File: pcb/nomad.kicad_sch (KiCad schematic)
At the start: 39 parts, among them J1 USB_C_Receptacle_USB2.0_16P, J5 Conn_01x02_Pin, SW1 UP, SW2 DOWN, SW3 RIGHT, SW4 LEFT, SW5 SEL, SW6 SW_Push, SW7 SW_Push, U1 ESP32-S3-WROOM-1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

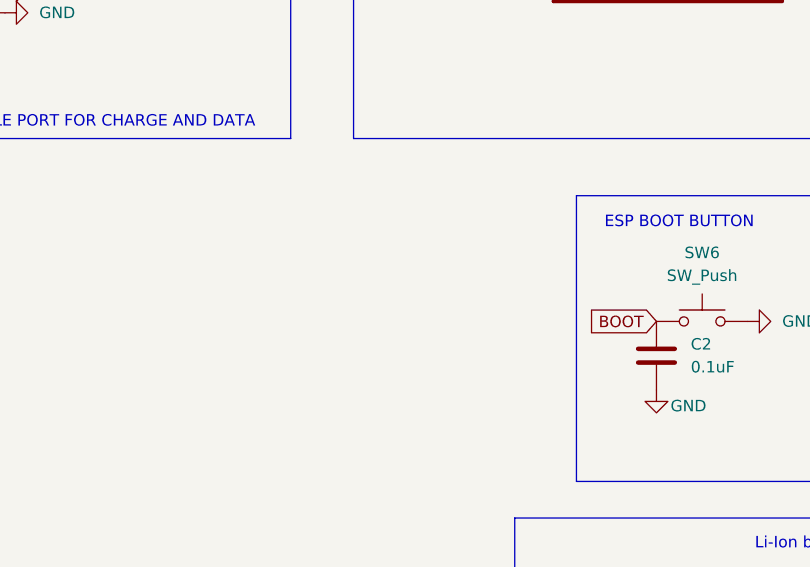
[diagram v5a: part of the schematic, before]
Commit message: Updating footprints, PCb and schematics.
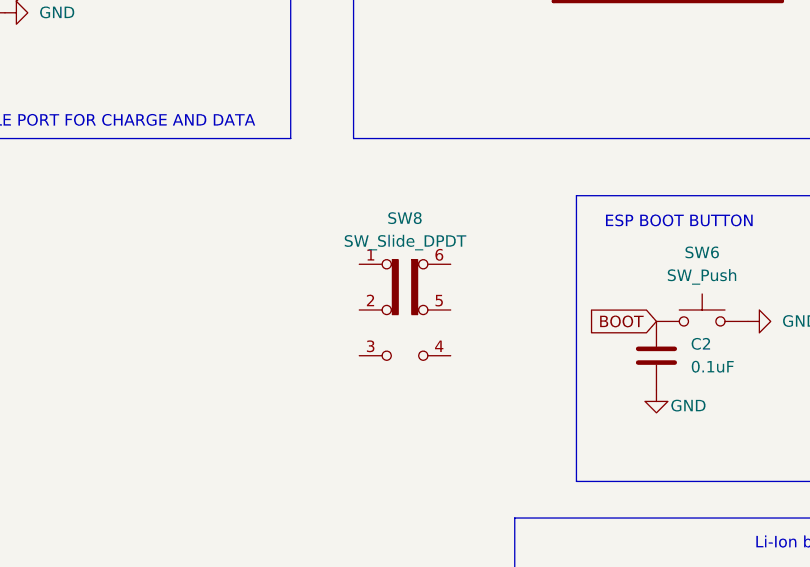
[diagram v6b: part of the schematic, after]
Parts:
- added SW8: SW_Slide_DPDT, symbol Switch:SW_Slide_DPDT
- C12: footprint (none) -> Capacitor_SMD:C_0805_2012Metric
- R18: footprint (none) -> Resistor_SMD:R_0805_2012Metric
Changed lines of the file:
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@@
 			)
 		)
-		(property "Footprint" ""
+		(property "Footprint" "Resistor_SMD:R_0805_2012Metric"
 			(at 225.552 127 90)
 			(hide yes)
@@
 			)
 		)
-		(property "Footprint" ""
+		(property "Footprint" "Capacitor_SMD:C_0805_2012Metric"
 			(at 164.7952 43.18 0)
 			(hide yes)
@@
 					(unit 1)
 				)
+			)
+		)
+	)
+	(symbol
+		(lib_id "Switch:SW_Slide_DPDT")
+		(at 95.25 92.71 0)
+		(unit 1)
+		(body_style 1)
+		(exclude_from_sim no)
+		(in_bom yes)
+		(on_board yes)
+		(in_pos_files yes)
+		(dnp no)
+		(fields_autoplaced yes)
+		(property "Reference" "SW8"
+			(at 95.25 82.55 0)
+			(show_name no)
+			(do_not_autoplace no)
+			(effects
+				(font
+					(size 1.27 1.27)
+				)
+			)
+		)
+		(property "Value" "SW_Slide_DPDT"
+			(at 95.25 85.09 0)
+			(show_name no)
+			(do_not_autoplace no)
+			(effects
+				(font
+					(size 1.27 1.27)
+				)
+			)
+		)
+		(property "Footprint" ""
+			(at 109.22 87.63 0)
+			(hide yes)
+			(show_name no)
+			(do_not_autoplace no)
+			(effects
+				(font
+					(size 1.27 1.27)
+				)
+			)
+		)
+		(property "Datasheet" ""
+			(at 95.25 92.71 0)
+			(hide yes)
+			(show_name no)
+			(do_not_autoplace no)
+			(effects
+				(font
+					(size 1.27 1.27)
+				)
+			)
+		)
+		(property "Description" "Slide Switch, dual pole double throw"
+			(at 95.25 92.71 0)
+			(hide yes)
+			(show_name no)
+			(do_not_autoplace no)
+			(effects
+				(font
+					(size 1.27 1.27)
+				)
+			)
+		)
+		(pin "1"
+		)
+		(pin "4"
+		)
+		(pin "2"
+		)
+		(pin "3"
+		)
+		(pin "6"
+		)
+		(pin "5"
+		)
+		(instances
+			(project "nomad"
+				(path "/76473bbd-feb6-4b7c-8160-a4d55fa11a55"
+					(reference "SW8")
+					(unit 1)
+				)

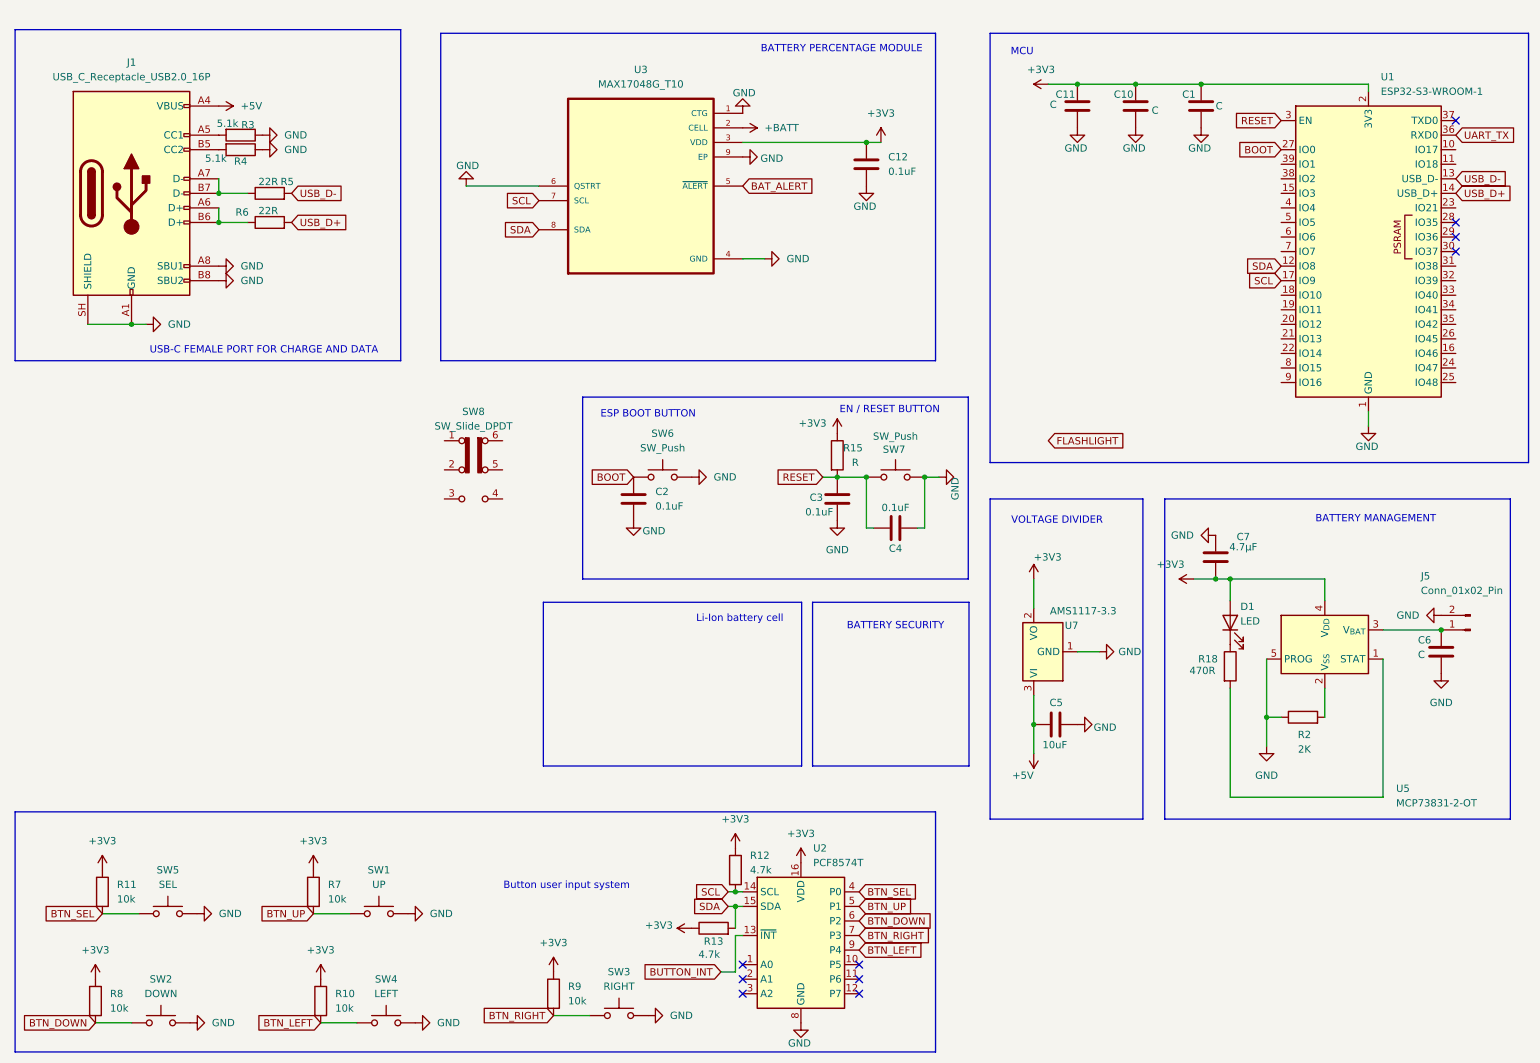
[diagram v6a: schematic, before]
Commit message: Updating PCB: Adding Buck boost converter, battery protection and other fixes.
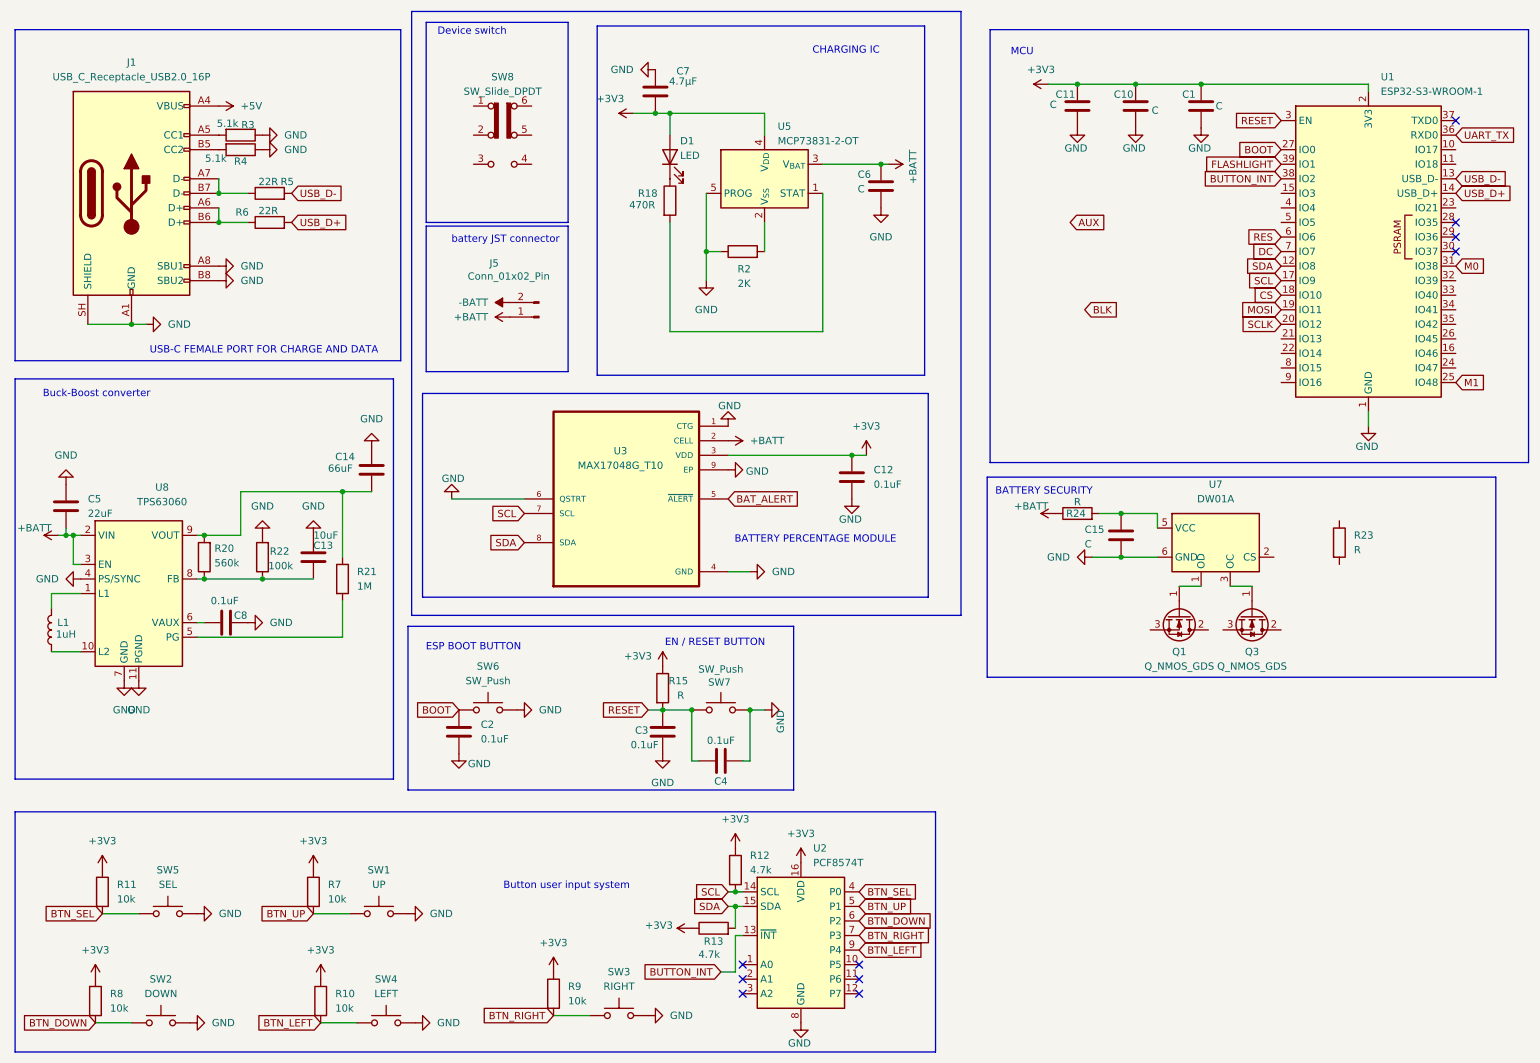
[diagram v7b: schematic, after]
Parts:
- removed U7: AMS1117-3.3, Package_TO_SOT_SMD:SOT-223-3_TabPin2, symbol Regulator_Linear:AMS1117-3.3
- added C13: 10uF, Capacitor_SMD:C_0805_2012Metric, symbol Device:C
- added C14: 66uF, Capacitor_SMD:C_0805_2012Metric, symbol Device:C
- added C15: C, symbol Device:C
- added C8: 0.1uF, Capacitor_SMD:C_0805_2012Metric, symbol Device:C
- added L1: 1uH, Inductor_SMD:L_Coilcraft_XxL4020, symbol Device:L
- added Q1, Q3: Q_NMOS_GDS, symbol Transistor_FET:Q_NMOS_GDS
- added R20: 560k, Resistor_SMD:R_0805_2012Metric, symbol Device:R
- added R21: 1M, Resistor_SMD:R_0805_2012Metric, symbol Device:R
- added R22: 100k, Resistor_SMD:R_0805_2012Metric, symbol Device:R
- added R23, R24: R, symbol Device:R
- added U7: DW01A, Package_TO_SOT_SMD:SOT-23-6, symbol Battery_Management:DW01A
- added U8: TPS63060, Package_SON:Texas_S-PWSON-N10_ThermalVias, symbol Regulator_Switching:TPS63060
- C1, C10, C11: footprint (none) -> Capacitor_SMD:C_0805_2012Metric
- C5: value 10uF -> 22uF
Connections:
- net +5V: no longer C5.1
- net +BATT: now also C5.2, C6.1, J5.1 (Pin_1), U5.3 (V_{BAT}), R24.1, U8.2 (VIN), U8.3 (EN)
- net BUTTON_INT: now also U1.38 (IO2)
- net FLASHLIGHT: now also U1.39 (IO1)
- net GND: now also C5.1, C13.1, C14.1, C15.2, C8.2, R22.2, U7.6 (GND), U8.11 (PGND), U8.4 (PS/SYNC), U8.7 (GND); no longer C5.2, J5.2 (Pin_2)
- net CS: now reaches U1.18 (IO10)
- net MOSI: now reaches U1.19 (IO11)
- net SCLK: now reaches U1.20 (IO12)
- net M1: now reaches U1.25 (IO48)
- net M0: now reaches U1.31 (IO38)
- net RES: now reaches U1.6 (IO6)
- net DC: now reaches U1.7 (IO7)
- new net: L1.2, U8.1 (L1)
- new net: L1.1, U8.10 (L2)
- new net: R21.2, U8.5 (PG)
- new net: C8.1, U8.6 (VAUX)
- new net: C13.2, R20.1, R22.1, U8.8 (FB)
- new net: C14.2, R20.2, R21.1, U8.9 (VOUT)
- new net: Q1.1 (G), U7.1 (OD)
- new net: Q3.1 (G), U7.3 (OC)
- new net: C15.1, R24.2, U7.5 (VCC)
- new net -BATT: J5.2 (Pin_2)
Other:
- note added: "Buck-Boost converter"
- note added: "CHARGING IC"
- note added: "Device switch"
- note added: "battery JST connector"
- note removed: "BATTERY MANAGEMENT"
- note removed: "Li-Ion battery cell"
- note removed: "VOLTAGE DIVIDER"
- moved on the sheet: C12, C2, C3, C4, C6, C7, D1, J5, R15, R18, R2, SW6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

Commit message: Updating PCB: Removing battery security and adding slide switch
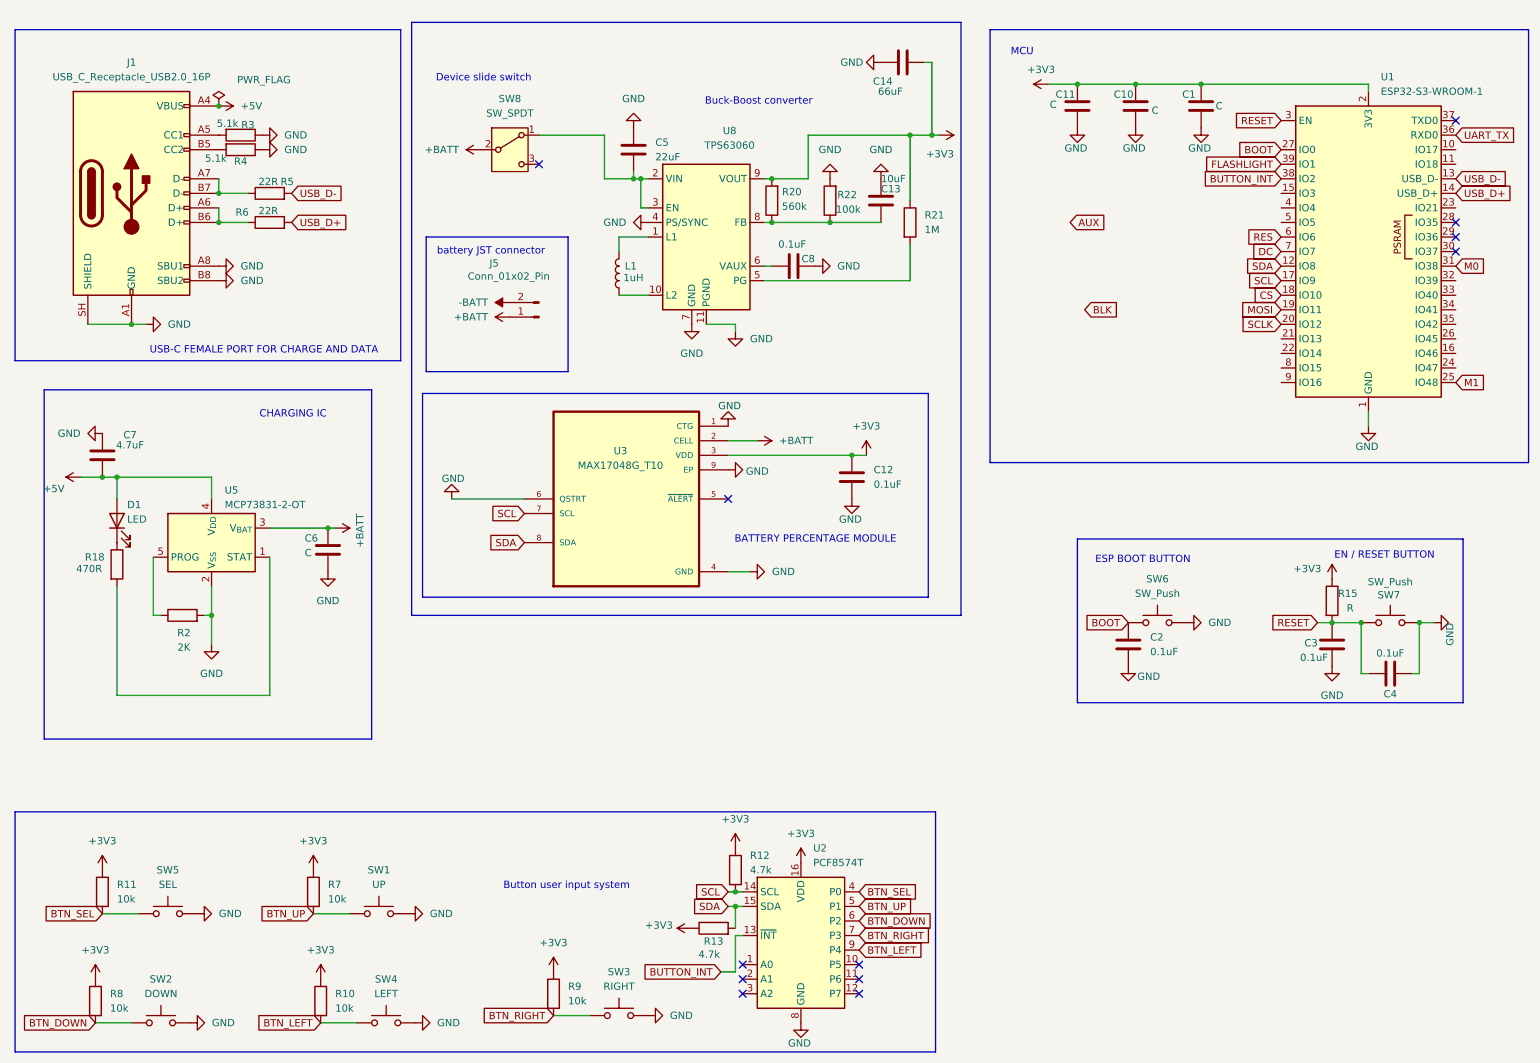
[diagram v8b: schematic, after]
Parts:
- removed C15: C, symbol Device:C
- removed Q1, Q3: Q_NMOS_GDS, symbol Transistor_FET:Q_NMOS_GDS
- removed R23, R24: R, symbol Device:R
- removed SW8: SW_Slide_DPDT, symbol Switch:SW_Slide_DPDT
- removed U7: DW01A, Package_TO_SOT_SMD:SOT-23-6, symbol Battery_Management:DW01A
- added SW8: SW_SPDT, Connector_PinHeader_1.00mm:PinHeader_1x03_P1.00mm_Horizontal, symbol Switch:SW_SPDT
- C7: value 4.7µF -> 4.7uF
- D1: footprint (none) -> LED_SMD:LED_0805_2012Metric
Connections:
- net +3V3: now also C14.2, R20.2, R21.1, U8.9 (VOUT); no longer C7.1, D1.2 (A), U5.4 (V_{DD})
- net +5V: now also C7.1, D1.2 (A), U5.4 (V_{DD})
- net +BATT: now also SW8.2 (B); no longer C5.2, U8.2 (VIN), U8.3 (EN)
- net GND: now also R2.2, U5.2 (V_{SS}); no longer R2.1, U5.5 (PROG)
- net BAT_ALERT: no longer names the net of U3.5 (~{ALERT})
- new net: C5.2, SW8.1 (A), U8.2 (VIN), U8.3 (EN)
- new net: R2.1, U5.5 (PROG)
- no-connect marks 10 -> 12
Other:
- note added: "Device slide switch"
- note removed: "BATTERY SECURITY"
- note removed: "Device switch"
- moved on the sheet: C13, C14, C2, C3, C4, C5, C6, C7, C8, D1, L1, R15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
